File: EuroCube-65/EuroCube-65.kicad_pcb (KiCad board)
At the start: 2 copper layers, 160 x 100 mm, 105 parts, among them CON1 SERIAL PORT, CON2 PARALLEL PORT, CON3 EXPANSION BUS, IC1 6551A, IC10 GAL16V8, IC11 6522, IC12 6502, IC13 7660, IC2 26LS30, IC3 M3002, IC4 26LS32, IC5 74LS04, IC7 74LS00, IC8 74HCT132, IC9 GAL16V8, T1 BC547, T2 2N7000, T3 2N3906, X1 1.843MHz, X2 32.768kHz, X3 1MHz

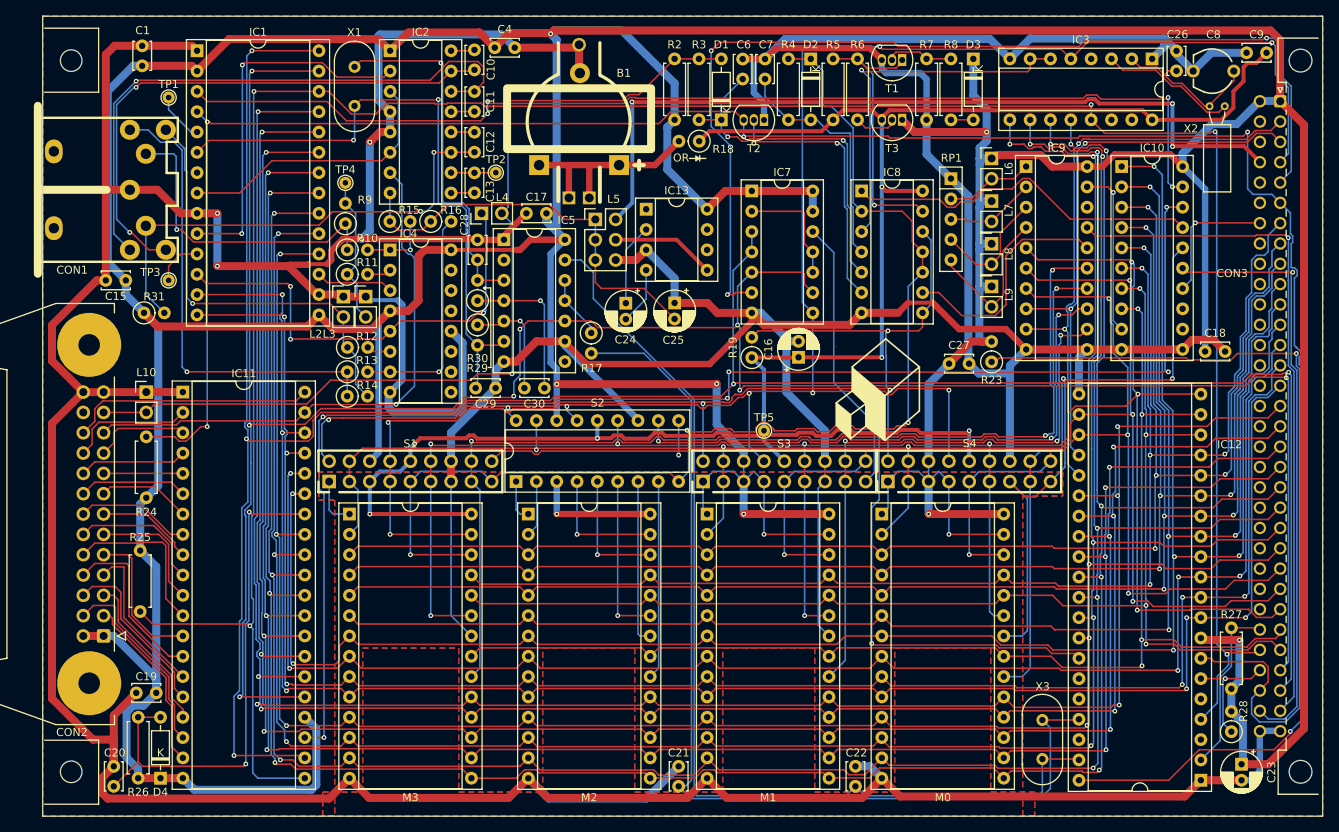
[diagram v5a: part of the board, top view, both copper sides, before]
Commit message: Tidying of unnecessary GND traces
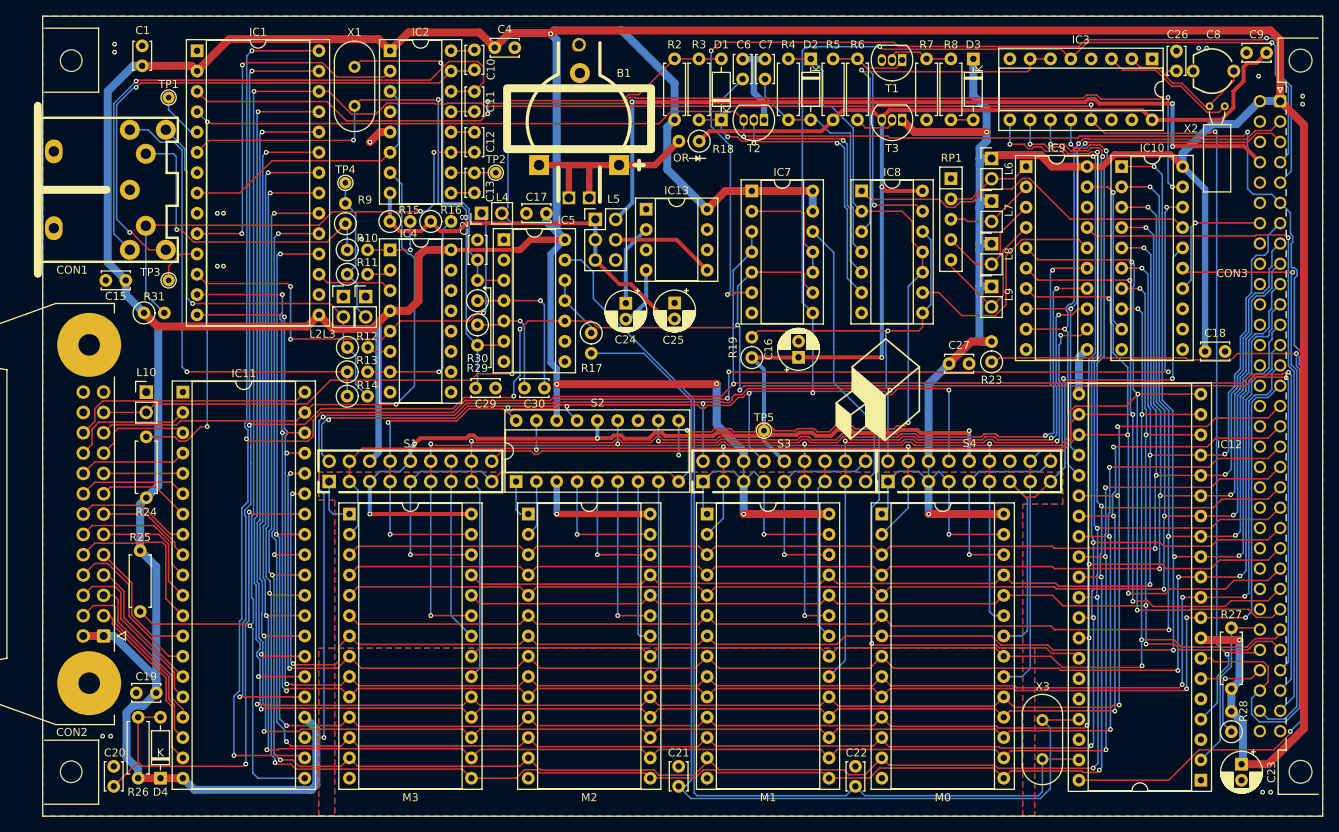
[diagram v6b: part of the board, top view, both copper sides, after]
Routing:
- net GND: track 891.8 -> 69.3 mm, vias 4 -> 17
- net Net-(CON2-Pin_7): track 19.7 -> 17.1 mm
- net Net-(IC2C-VEE): track 51.4 -> 49.4 mm
- net Net-(CON2-Pin_9): track 18.3 -> 16.5 mm
- net Net-(CON2-Pin_8): track 21.5 -> 20.1 mm

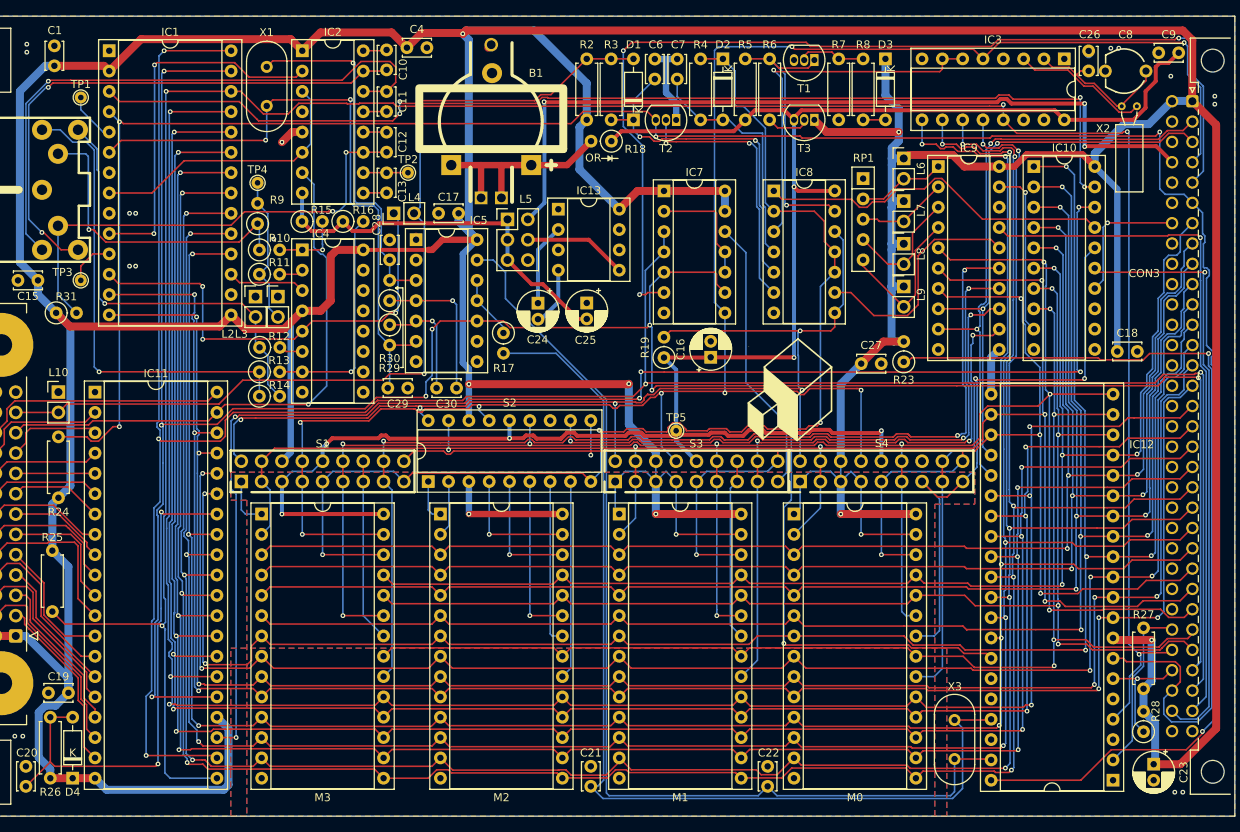
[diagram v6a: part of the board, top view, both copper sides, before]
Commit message: Minor footprint tweaks
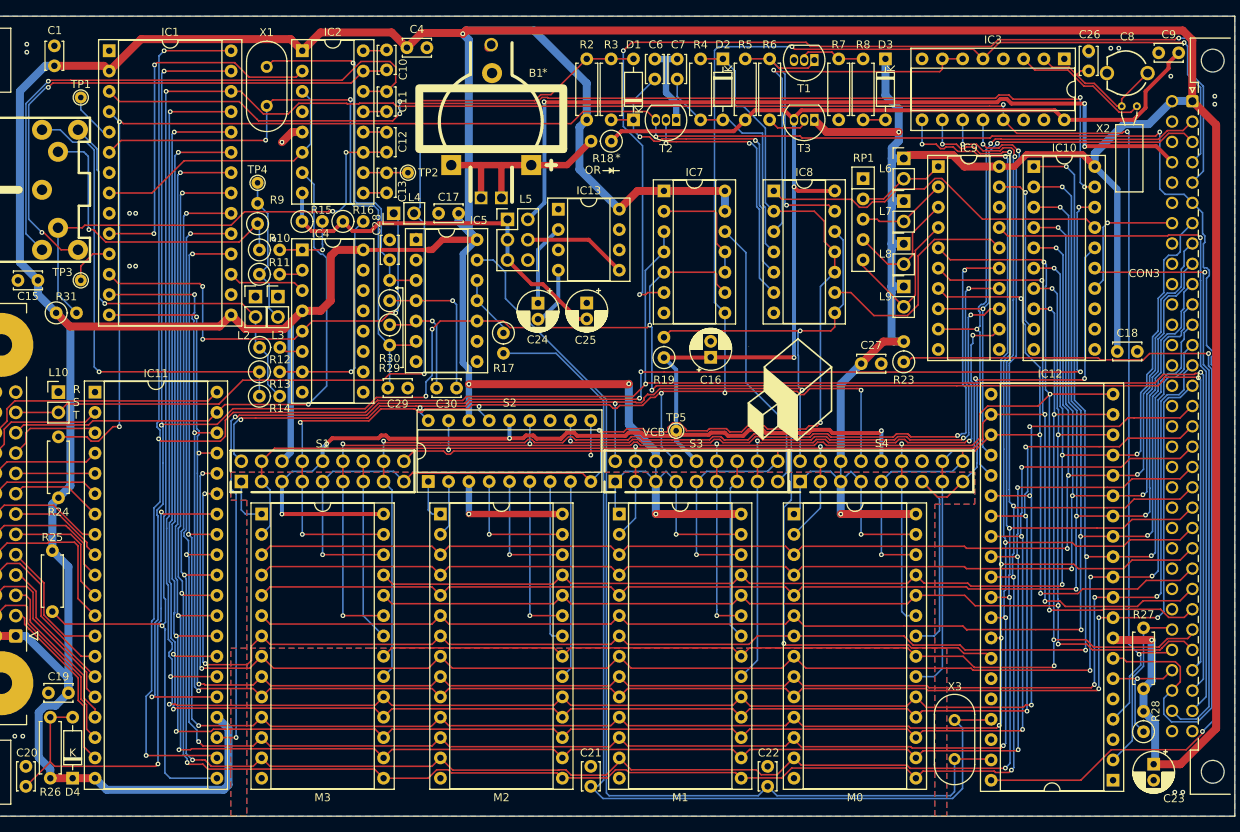
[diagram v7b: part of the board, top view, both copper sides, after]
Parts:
- moved C8 0.33 mm to (198.9, 54.9)
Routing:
- net GND: track 69.3 -> 63.3 mm
- net /VCB: track 250.3 -> 249.7 mm
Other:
- board text added: "*"
- board text added: "*If coin cell used for B1 replace R18 with 1N4148"
- board text added: "EuroBEEB Single Board Computer Issue 8 steve@croz.co.uk 2024-12-29"
- board text added: "R S T"
- board text added: "See manual/schematic for configuration links and optional part fitment"
- board text added: "VCB"
- board text removed: "EuroBEEB Single Board Computer Issue 8 steve@croz.co.uk Dec 28 2024"
